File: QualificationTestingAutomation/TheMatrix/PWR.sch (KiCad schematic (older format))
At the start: 94 parts, among them J13 Barrel_Jack_MountingPin, J14 Banana Jack, J15 Banana Jack, Q1 ULN2003ADR, Q2 ULN2003ADR, U27 LM2776, U4 TPS563210, U5 TPS563210, U6 LM2776

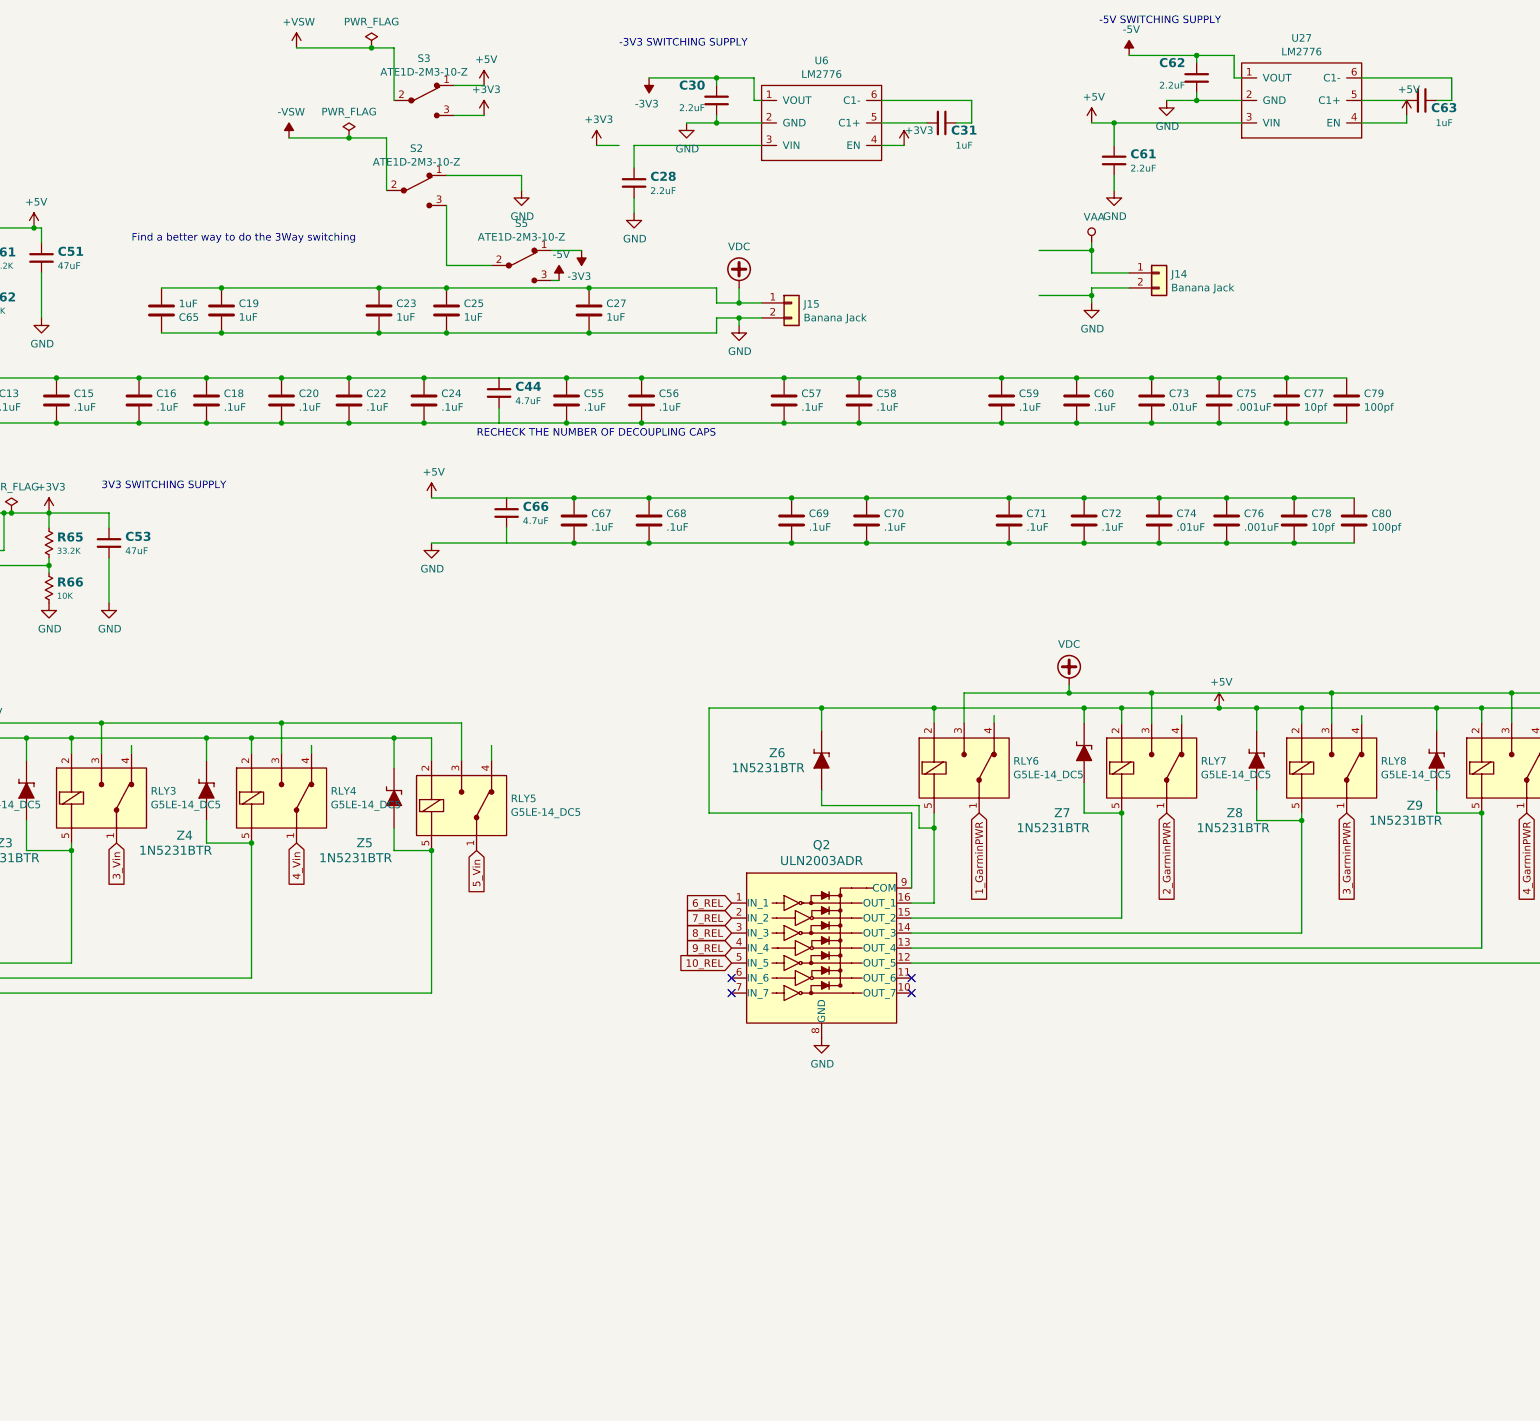
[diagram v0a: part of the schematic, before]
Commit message: Added 60V supply for the MUX's so they can be independent from Vpower, Added another seperate power rail
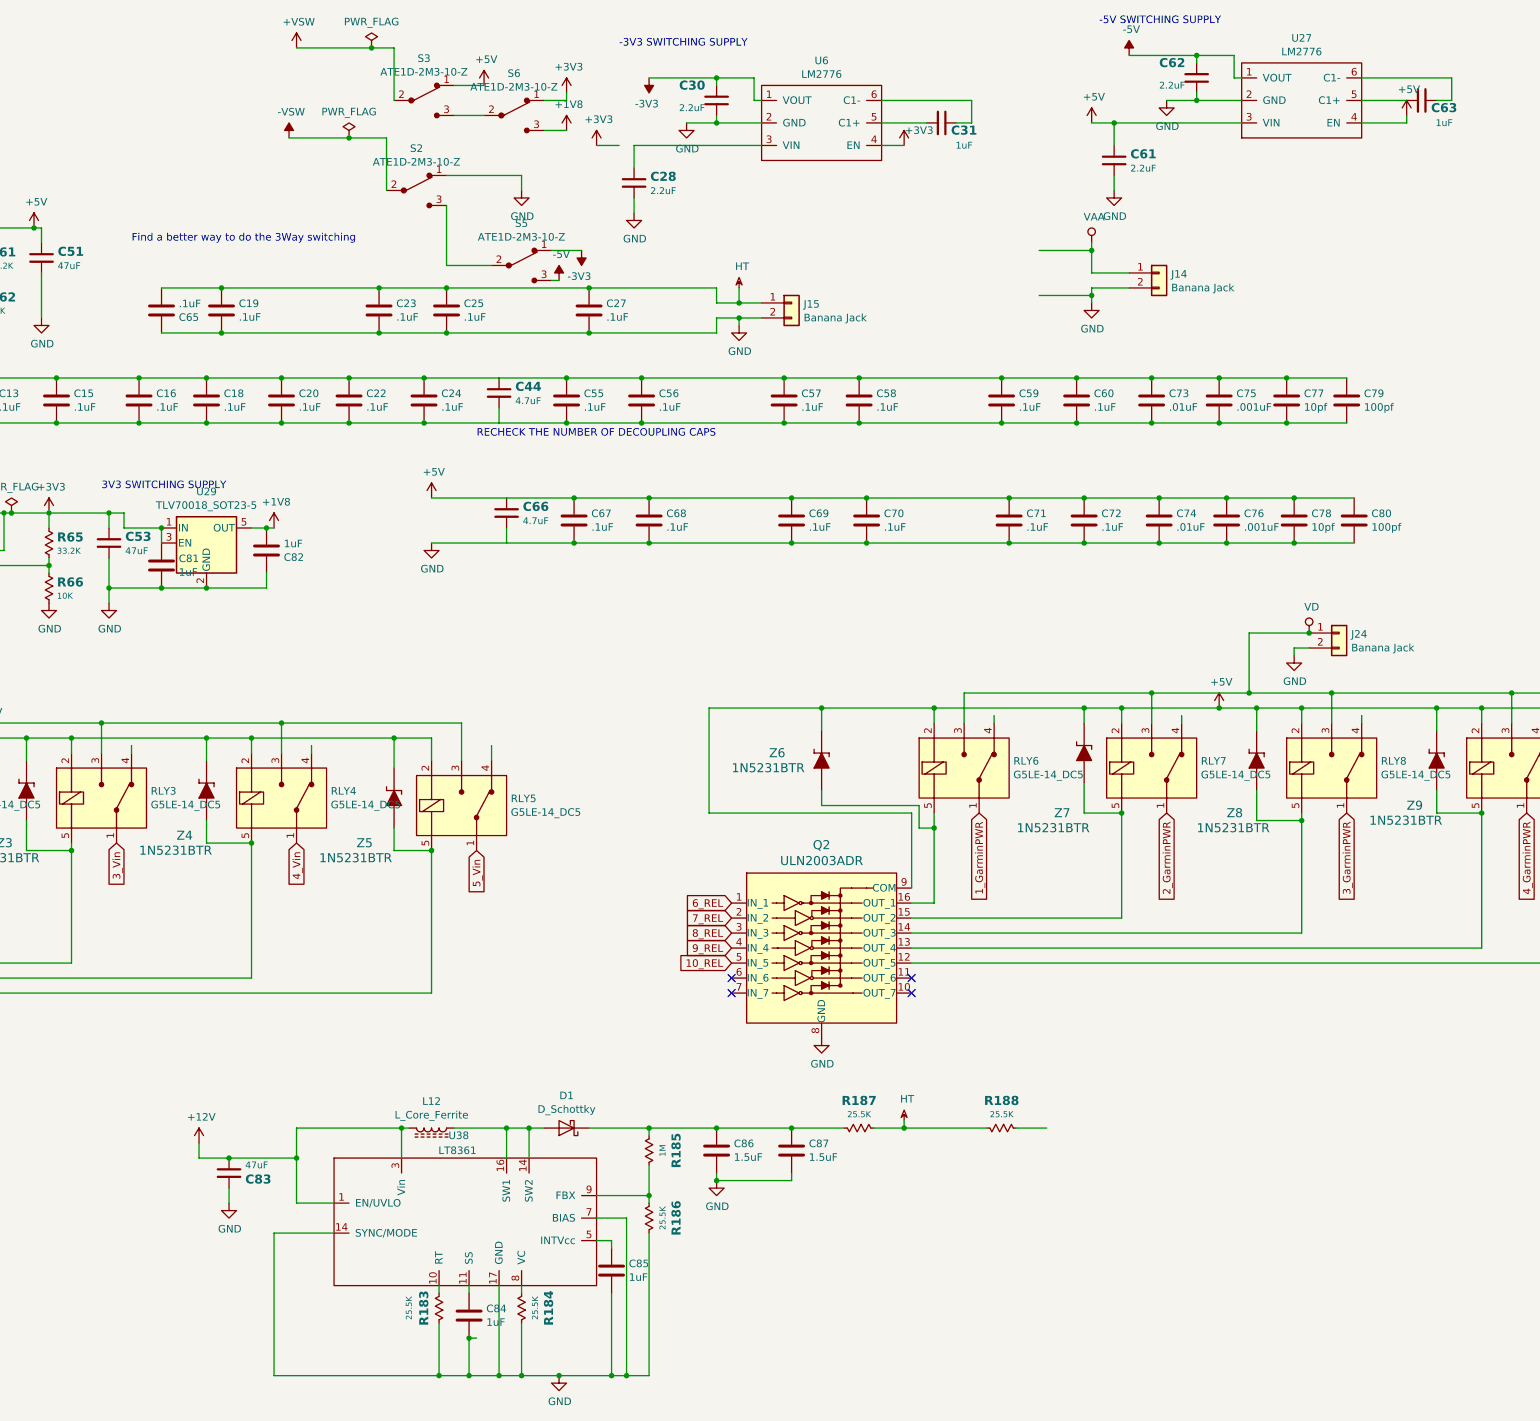
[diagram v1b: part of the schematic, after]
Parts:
- added C81, C82: 1uF, Capacitor_SMD:C_1206_3216Metric_Pad1.42x1.75mm_HandSolder, symbol Device:C
- added C83: 47uF, Capacitor_SMD:C_1210_3225Metric_Pad1.42x2.65mm_HandSolder, symbol TheMatrix-rescue:CAP-passive-SchematicAutomation-rescue
- added C84: 1uF, Capacitor_SMD:C_0201_0603Metric, symbol Device:C
- added C85: 1uF, Capacitor_SMD:C_0603_1608Metric_Pad1.05x0.95mm_HandSolder, symbol Device:C
- added C86, C87: 1.5uF, Capacitor_SMD:C_1206_3216Metric_Pad1.42x1.75mm_HandSolder, symbol Device:C
- added D1: D_Schottky, Diode_SMD:D_PowerDI-123, symbol Device:D_Schottky
- added J24: Banana Jack, Connector:Banana_Jack_2Pin_Standard_Spacing, symbol Connector_Generic:Conn_01x02
- added L12: L_Core_Ferrite, Inductor_SMD:L_Wuerth_WE-PD-Typ-LS_Handsoldering, symbol Device:L_Core_Ferrite
- added R183, R184, R186: 25.5K, Resistor_SMD:R_0402_1005Metric, symbol TheMatrix-rescue:RESISTOR-passive-SchematicAutomation-rescue
- added R185: 1M, Resistor_SMD:R_0805_2012Metric_Pad1.15x1.40mm_HandSolder, symbol TheMatrix-rescue:RESISTOR-passive-SchematicAutomation-rescue
- added R187: 25.5K, Resistor_SMD:R_1210_3225Metric_Pad1.42x2.65mm_HandSolder, symbol TheMatrix-rescue:RESISTOR-passive-SchematicAutomation-rescue
- added R188: 25.5K, Resistor_SMD:R_1210_3225Metric, symbol TheMatrix-rescue:RESISTOR-passive-SchematicAutomation-rescue
- added S6: ATE1D-2M3-10-Z, digikey-footprints:Switch_Toggle_ATE1D-2M3-10-Z, symbol TheMatrix-rescue:ATE1D-2M3-10-Z-dk_Toggle-Switches-SchematicAutomation-rescue
- added U29: TLV70018_SOT23-5, Package_TO_SOT_SMD:SOT-23-5, symbol Regulator_Linear:TLV70018_SOT23-5
- added U38: LT8361, Package_SO:MSOP-12-16-1EP_3x4mm_P0.5mm_EP1.65x2.85mm, symbol BoostConverters:LT8361
- C19, C23, C25, C27, C65: value 1uF -> .1uF
- J14, J15: footprint Connectors:Banana_Jack_2Pin -> Connector:Banana_Jack_2Pin_Standard_Spacing
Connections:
- net labels added: +1V8, HT, VD
- wire segments 339 -> 410

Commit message: Major upgrade, Finished laying out switcheroo, and the Matrix.
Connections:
- wire segments 410 -> 412
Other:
- moved on the sheet: J15
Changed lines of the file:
@@
 EESchema Schematic File Version 4
-LIBS:TheMatrix-cache
 EELAYER 26 0
 EELAYER END
@@
 L Connector_Generic:Conn_01x02 J?
 U 1 1 5BE1D7EC
-P 9500 2450
+P 9900 2450
 AR Path="/5BE1D7EC" Ref="J?"  Part="1"
 AR Path="/5B9C8971/5BE1D7EC" Ref="J?"  Part="1"
 AR Path="/5BA2CD36/5BE1D7EC" Ref="J15"  Part="1"
-F 0 "J15" H 9580 2442 50  0000 L CNN
-F 1 "Banana Jack" H 9580 2351 50  0000 L CNN
-F 2 "Connector:Banana_Jack_2Pin_Standard_Spacing" H 9500 2450 50  0001 C CNN
-F 3 "~" H 9500 2450 50  0001 C CNN
-F 4 "The hole has a diameter of about 5.2mm (fits standard 4mm banana plugs), the cap on the front has an outside diameter of about 11.6mm and length of 15.2mm. Diameter of the screw is 3.8mm. The mounting key is about 4 x 5.4mm." H -950 150 50  0001 C CNN "Description"
-	1    9500 2450
+F 0 "J15" H 9980 2442 50  0000 L CNN
+F 1 "Banana Jack" H 9980 2351 50  0000 L CNN
+F 2 "Connector:Banana_Jack_2Pin_Standard_Spacing" H 9900 2450 50  0001 C CNN
+F 3 "~" H 9900 2450 50  0001 C CNN
+F 4 "The hole has a diameter of about 5.2mm (fits standard 4mm banana plugs), the cap on the front has an outside diameter of about 11.6mm and length of 15.2mm. Diameter of the screw is 3.8mm. The mounting key is about 4 x 5.4mm." H -550 150 50  0001 C CNN "Description"
+	1    9900 2450
 	1    0    0    -1
 $EndComp
@@
 $EndComp
 Wire Wire Line
-	9300 2550 9150 2550
+	9700 2550 9550 2550
 Wire Wire Line
 	9150 2550 9150 2600
@@
 $EndComp
 Wire Wire Line
-	9150 2450 9300 2450
+	9550 2450 9700 2450
 $Comp
 L power:-3V3 #PWR0330
@@
 Wire Wire Line
 	9000 2450 9000 2350
-Connection ~ 9150 2450
 Wire Wire Line
 	9150 2550 9000 2550
 Wire Wire Line
 	9000 2550 9000 2650
-Connection ~ 9150 2550
 Wire Wire Line
 	8150 2350 9000 2350
@@
 	9000 7950 9500 7950
 $Comp
-L power:HT #PWR?
+L power:HT #PWR0328
 U 1 1 5D871F4F
 P 9150 2350
-F 0 "#PWR?" H 9150 2470 50  0001 C CNN
+F 0 "#PWR0328" H 9150 2470 50  0001 C CNN
 F 1 "HT" H 9170 2493 50  0000 C CNN
 F 2 "" H 9150 2350 50  0001 C CNN
@@
 	1    0    0    -1
 $EndComp
+$Comp
+L power:VDC #PWR0348
+U 1 1 5D8CFECA
+P 9550 2450
+F 0 "#PWR0348" H 9550 2350 50  0001 C CNN
+F 1 "VDC" H 9550 2725 50  0000 C CNN
+F 2 "" H 9550 2450 50  0001 C CNN
+F 3 "" H 9550 2450 50  0001 C CNN
+	1    9550 2450
+	1    0    0    -1
+$EndComp
+Wire Wire Line
+	9550 2550 9550 2600
+Wire Wire Line
+	9550 2600 9150 2600
+Connection ~ 9150 2600
 $EndSCHEMATC
